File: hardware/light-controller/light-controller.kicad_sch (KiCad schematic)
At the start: 124 parts, among them J1 BATT 4S-6S, J2 USB-C, J3 SWD, J4 UART to FC, M1 RM2, Q1 DMP6023LE, SW1 BOOTSEL, U1 LMR51420YDDCR, U2 RP2350A, U3 W25Q16JVSNIQ, U4 USBLC6-2SC6, U5 AL8860MP-13, U6 AL8860MP-13, U7 AL8860MP-13, U8 AL8860MP-13, Y1 12MHz

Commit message: light-controller: LED array per colour row, no USB, routing tools, README (WIP)
Co-Authored-By: Claude Opus 5.5 (1M context) <noreply@anthropic.com>
Claude-Session: https://claude.ai/code/session_01KXRTPSv3xMSgDNs8D9aXZS
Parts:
- removed D3: B5819W, lightctl:D_SOD-123, symbol lightctl:D_Schottky
- removed J2: USB-C, lightctl:USB_C_Receptacle_GCT_USB4105-xx-A_16P_TopMnt_Horizontal, symbol lightctl:USB_C_16P
- removed R10: 1k, lightctl:R_0603_1608Metric, symbol lightctl:R
- removed R12, R13: 5.1k, lightctl:R_0603_1608Metric, symbol lightctl:R
- removed R14, R15: 27, lightctl:R_0603_1608Metric, symbol lightctl:R
- removed R9: 10k, lightctl:R_0603_1608Metric, symbol lightctl:R
- removed SW1: BOOTSEL, lightctl:SW_SPST_PTS810, symbol lightctl:SW_Push
- removed TP5: GPIO28, lightctl:TestPoint_Pad_D1.5mm, symbol lightctl:TestPoint
- removed U4: USBLC6-2SC6, lightctl:SOT-23-6, symbol lightctl:USBLC6-2SC6
- TP2: value GPIO8 -> GPIO10
- TP3: value GPIO9 -> GPIO11
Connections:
- net PWM_B: now also U2.13 (GPIO9); no longer U2.7 (GPIO4)
- net PWM_G: now also U2.4 (GPIO2); no longer U2.5 (GPIO3)
- net PWM_R: now also U2.12 (GPIO8); no longer U2.4 (GPIO2)
- net PWM_W: now also U2.5 (GPIO3); no longer U2.8 (GPIO5)
- net GPIO10: now reaches U2.14 (GPIO10)
- net GPIO10: now also TP2.1
- net GPIO11: now reaches U2.15 (GPIO11)
- net GPIO11: now also TP3.1
- net GPIO28: no longer names the net of U2.42 (GPIO28_ADC2)
- removed net GPIO8: TP2.1, U2.12 (GPIO8)
- removed net GPIO9: TP3.1, U2.13 (GPIO9)
- net USB_DM: no longer names the net of U2.51 (USB_DM)
- net USB_DP: no longer names the net of U2.52 (USB_DP)
- no-connect marks 24 -> 25
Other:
- moved on the sheet: C31, C32, C33, C34, C41, C42, C43, C44, C5, C51, C52, C53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

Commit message: light-controller: finish routing, pass DRC, add fab outputs
All nets routed on 2 layers with 0 DRC errors against the PCBWay rules
(silkscreen warnings only). Ground islands are stitched to the main pour,
leftover rip-up stubs are removed, and the board netlist matches design.py
pad for pad. Adds the gerber zip, BOM and placement file for PCBWay, fresh
renders, and README notes on DRC, spare pins and the status LED.

Co-Authored-By: Claude Opus 5.5 (1M context) <noreply@anthropic.com>
Claude-Session: https://claude.ai/code/session_01KXRTPSv3xMSgDNs8D9aXZS
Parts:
- removed D5: green, lightctl:LED_0603_1608Metric, symbol lightctl:LED
- removed R21: 1k, lightctl:R_0603_1608Metric, symbol lightctl:R
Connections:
- net STAT_LED: no longer names the net of U2.9 (GPIO6)
- no-connect marks 25 -> 26
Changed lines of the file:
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@@
   (no_connect (at 228.6 53.34))
   (no_connect (at 228.6 55.88))
-  (wire (pts (xy 228.6 58.42) (xy 231.14 58.42)) (stroke (width 0) (type default)))
-  (label "STAT_LED" (at 231.14 58.42 0) (fields_autoplaced) (effects (font (size 1.27 1.27)) (justify left bottom)))
+  (no_connect (at 228.6 58.42))
   (no_connect (at 228.6 60.96))
   (wire (pts (xy 228.6 63.5) (xy 231.14 63.5)) (stroke (width 0) (type default)))
@@
   (wire (pts (xy 278.13 101.6) (xy 280.67 101.6)) (stroke (width 0) (type default)))
   (label "RUN" (at 280.67 101.6 0) (fields_autoplaced) (effects (font (size 1.27 1.27)) (justify left bottom)))
-  (symbol (lib_id "lightctl:R") (at 281.94 114.3 0) (unit 1)
-    (in_bom yes) (on_board yes) (dnp no)
-    (property "Reference" "R21" (at 281.94 110.49 0) (effects (font (size 1.27 1.27))))
-    (property "Value" "1k" (at 281.94 118.11 0) (effects (font (size 1.27 1.27))))
-    (property "Footprint" "lightctl:R_0603_1608Metric" (at 281.94 114.3 0) (effects (font (size 1.27 1.27)) hide))
-    (property "Datasheet" "~" (at 281.94 114.3 0) (effects (font (size 1.27 1.27)) hide))
-    (property "Manufacturer" "Yageo" (at 281.94 114.3 0) (effects (font (size 1.27 1.27)) hide))
-    (property "MPN" "RC0603FR-071KL" (at 281.94 114.3 0) (effects (font (size 1.27 1.27)) hide))
-    (property "Side" "top" (at 281.94 114.3 0) (effects (font (size 1.27 1.27)) hide))
-    (pin "1")
-    (pin "2")
-    (instances (project "light-controller" (path "/7d07546c-1a33-5ef6-ab6f-da2278970f56" (reference "R21") (unit 1))))
-  )
-  (wire (pts (xy 278.13 114.3) (xy 275.59 114.3)) (stroke (width 0) (type default)))
-  (label "STAT_LED" (at 275.59 114.3 180) (fields_autoplaced) (effects (font (size 1.27 1.27)) (justify right bottom)))
-  (wire (pts (xy 285.75 114.3) (xy 288.29 114.3)) (stroke (width 0) (type default)))
-  (label "STAT_LED_A" (at 288.29 114.3 0) (fields_autoplaced) (effects (font (size 1.27 1.27)) (justify left bottom)))
-  (symbol (lib_id "lightctl:LED") (at 281.94 127 0) (unit 1)
-    (in_bom yes) (on_board yes) (dnp no)
-    (property "Reference" "D5" (at 281.94 123.19 0) (effects (font (size 1.27 1.27))))
-    (property "Value" "green" (at 281.94 130.81 0) (effects (font (size 1.27 1.27))))
-    (property "Footprint" "lightctl:LED_0603_1608Metric" (at 281.94 127 0) (effects (font (size 1.27 1.27)) hide))
-    (property "Datasheet" "~" (at 281.94 127 0) (effects (font (size 1.27 1.27)) hide))
-    (property "Manufacturer" "Wurth Elektronik" (at 281.94 127 0) (effects (font (size 1.27 1.27)) hide))
-    (property "MPN" "150060GS75000" (at 281.94 127 0) (effects (font (size 1.27 1.27)) hide))
-    (property "Side" "top" (at 281.94 127 0) (effects (font (size 1.27 1.27)) hide))
-    (pin "1")
-    (pin "2")
-    (instances (project "light-controller" (path "/7d07546c-1a33-5ef6-ab6f-da2278970f56" (reference "D5") (unit 1))))
-  )
-  (wire (pts (xy 278.13 127) (xy 275.59 127)) (stroke (width 0) (type default)))
-  (label "GND" (at 275.59 127 180) (fields_autoplaced) (effects (font (size 1.27 1.27)) (justify right bottom)))
-  (wire (pts (xy 285.75 127) (xy 288.29 127)) (stroke (width 0) (type default)))
-  (label "STAT_LED_A" (at 288.29 127 0) (fields_autoplaced) (effects (font (size 1.27 1.27)) (justify left bottom)))
   (symbol (lib_id "lightctl:Conn_1x03") (at 363.22 45.72 0) (unit 1)
     (in_bom yes) (on_board yes) (dnp no)

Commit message: light-controller: vertical SWD connector so the probe plugs in from below
The horizontal JST-SH on the bottom opened toward the middle of the board,
so the probe plug and cable ran into the parts around it, and the long edges
are inside the rail so it can't face outward. J3 is now a BM03B-SRSS-TB
vertical with the signal pads where they were; SWCLK, SWDIO and GPIO11 are
re-routed around it. DRC still 0 errors.

Co-Authored-By: Claude Opus 5.5 (1M context) <noreply@anthropic.com>
Claude-Session: https://claude.ai/code/session_01KXRTPSv3xMSgDNs8D9aXZS
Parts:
- J3: footprint lightctl:JST_SH_SM03B-SRSS-TB_1x03-1MP_P1.00mm_Horizontal -> lightctl:JST_SH_BM03B-SRSS-TB_1x03-1MP_P1.00mm_Vertical; MPN SM03B-SRSS-TB(LF)(SN) -> BM03B-SRSS-TB(LF)(SN)
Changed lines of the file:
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@@
     (property "Reference" "J3" (at 363.22 39.37 0) (effects (font (size 1.27 1.27))))
     (property "Value" "SWD" (at 363.22 52.07 0) (effects (font (size 1.27 1.27))))
-    (property "Footprint" "lightctl:JST_SH_SM03B-SRSS-TB_1x03-1MP_P1.00mm_Horizontal" (at 363.22 45.72 0) (effects (font (size 1.27 1.27)) hide))
+    (property "Footprint" "lightctl:JST_SH_BM03B-SRSS-TB_1x03-1MP_P1.00mm_Vertical" (at 363.22 45.72 0) (effects (font (size 1.27 1.27)) hide))
     (property "Datasheet" "~" (at 363.22 45.72 0) (effects (font (size 1.27 1.27)) hide))
     (property "Manufacturer" "JST" (at 363.22 45.72 0) (effects (font (size 1.27 1.27)) hide))
-    (property "MPN" "SM03B-SRSS-TB(LF)(SN)" (at 363.22 45.72 0) (effects (font (size 1.27 1.27)) hide))
+    (property "MPN" "BM03B-SRSS-TB(LF)(SN)" (at 363.22 45.72 0) (effects (font (size 1.27 1.27)) hide))
     (property "Side" "top" (at 363.22 45.72 0) (effects (font (size 1.27 1.27)) hide))
     (pin "1")

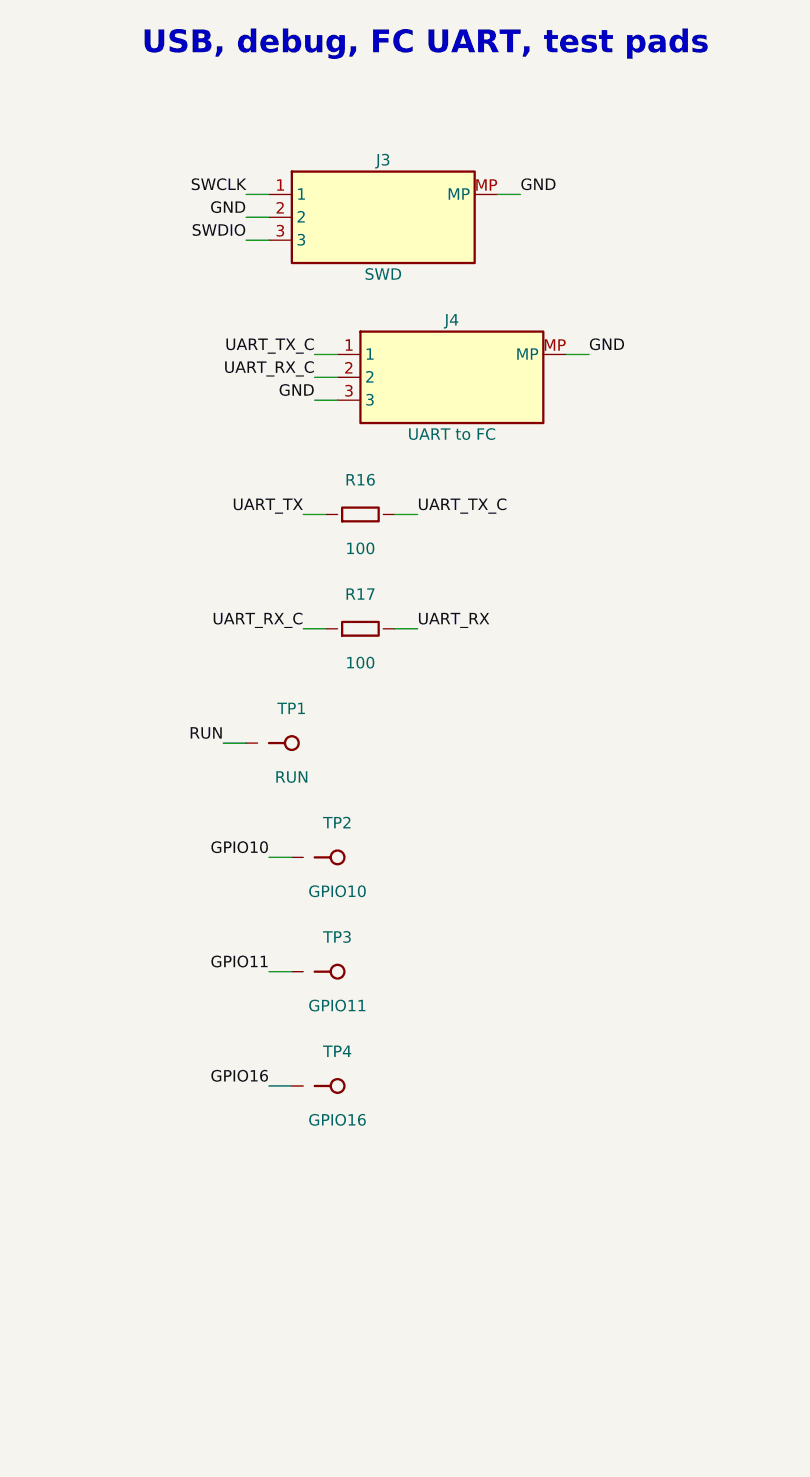
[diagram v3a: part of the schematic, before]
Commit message: light-controller: drop the SWD connector, program through pogo-pin pads
J3 is gone. SWCLK, GND and SWDIO are now test pads TP5-TP7 in the same
2.6 mm row as RUN and the spare GPIOs, so one pogo jig reaches all seven.
GPIO10/11 and the SWD nets are re-routed around the new pads; DRC is
still 0 errors and the netlist matches design.py.

Co-Authored-By: Claude Opus 5.5 (1M context) <noreply@anthropic.com>
Claude-Session: https://claude.ai/code/session_01KXRTPSv3xMSgDNs8D9aXZS
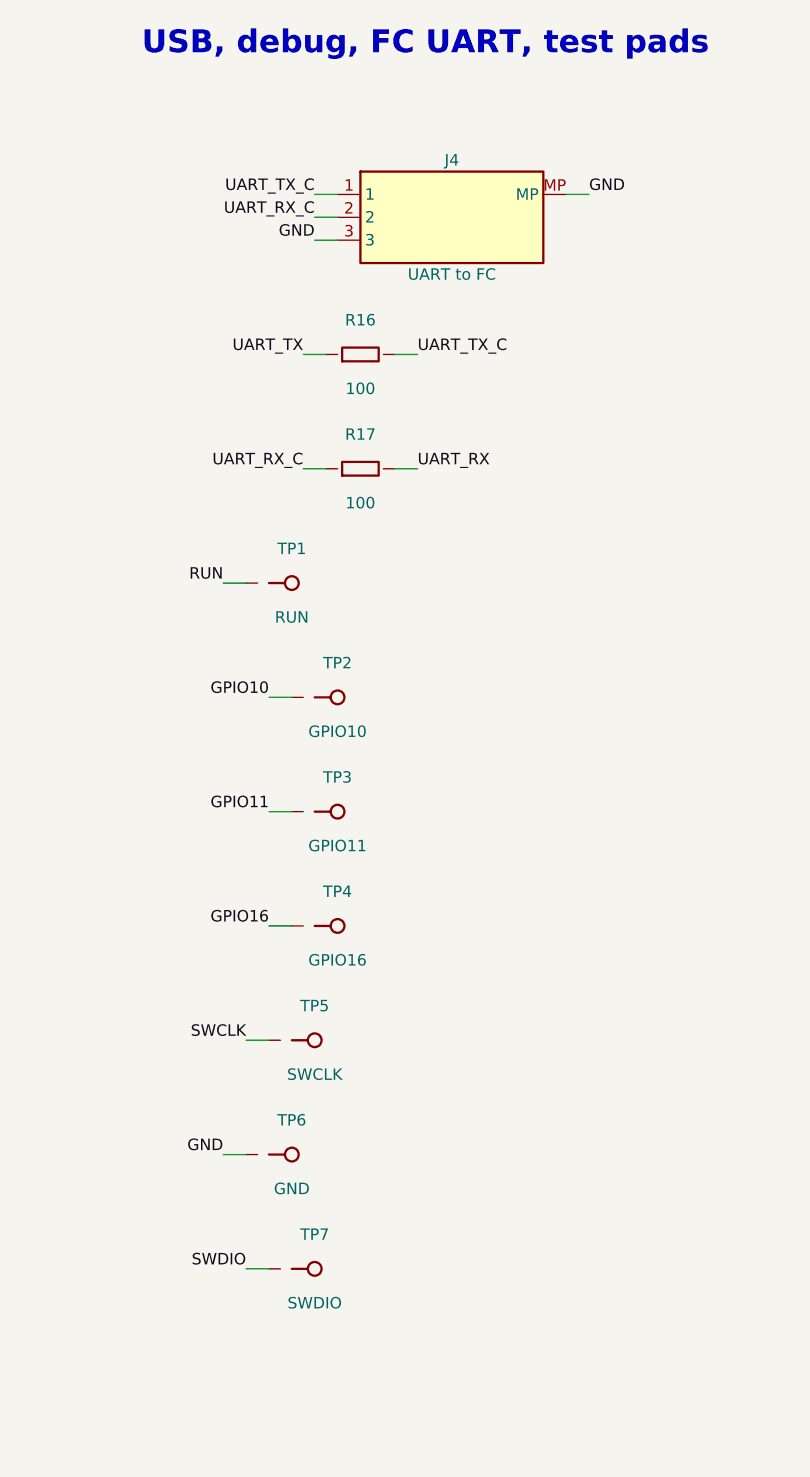
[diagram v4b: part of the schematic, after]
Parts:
- removed J3: SWD, lightctl:JST_SH_BM03B-SRSS-TB_1x03-1MP_P1.00mm_Vertical, symbol lightctl:Conn_1x03
- added TP5: SWCLK, lightctl:TestPoint_Pad_D1.5mm, symbol lightctl:TestPoint
- added TP6: GND, lightctl:TestPoint_Pad_D1.5mm, symbol lightctl:TestPoint
- added TP7: SWDIO, lightctl:TestPoint_Pad_D1.5mm, symbol lightctl:TestPoint
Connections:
- net GND: now also TP6.1
- net SWCLK: now also TP5.1
- net SWDIO: now also TP7.1
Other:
- moved on the sheet: J4, R16, R17, TP1, TP2, TP3, TP4
